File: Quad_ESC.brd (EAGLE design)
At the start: 96.5 x 39.9 mm, 28 parts, among them Y1 ECS-80-S-4X

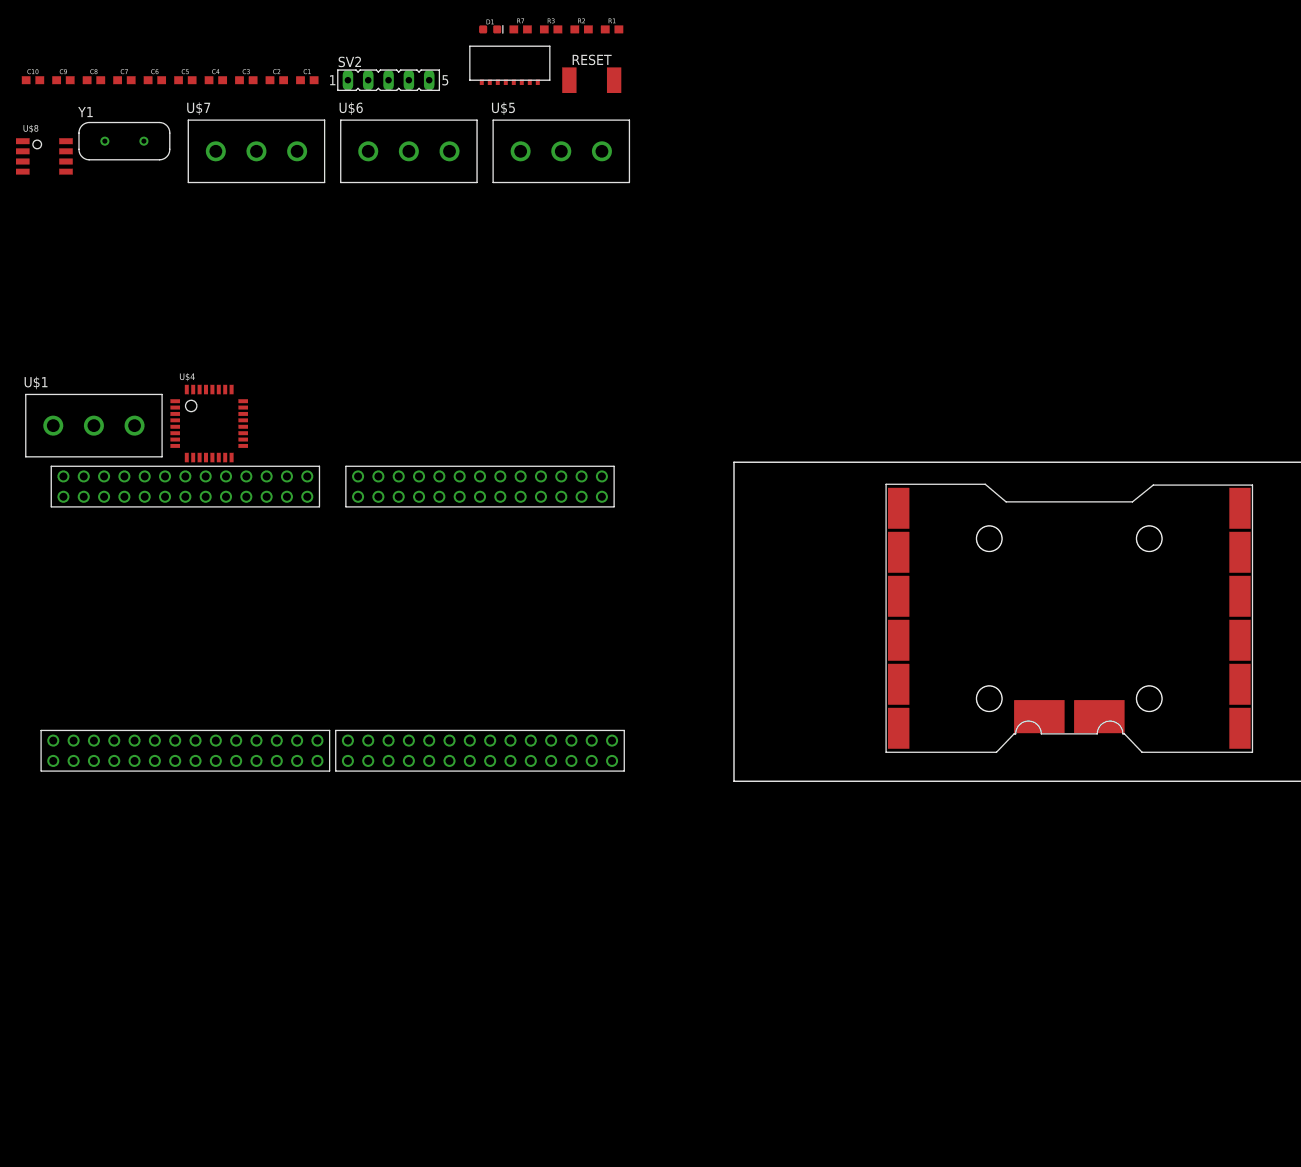
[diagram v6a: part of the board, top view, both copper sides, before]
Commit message: Schem/Lib Update
added new footprint to schematic and library, added ID resistor to chip, standardized symbols across schematic
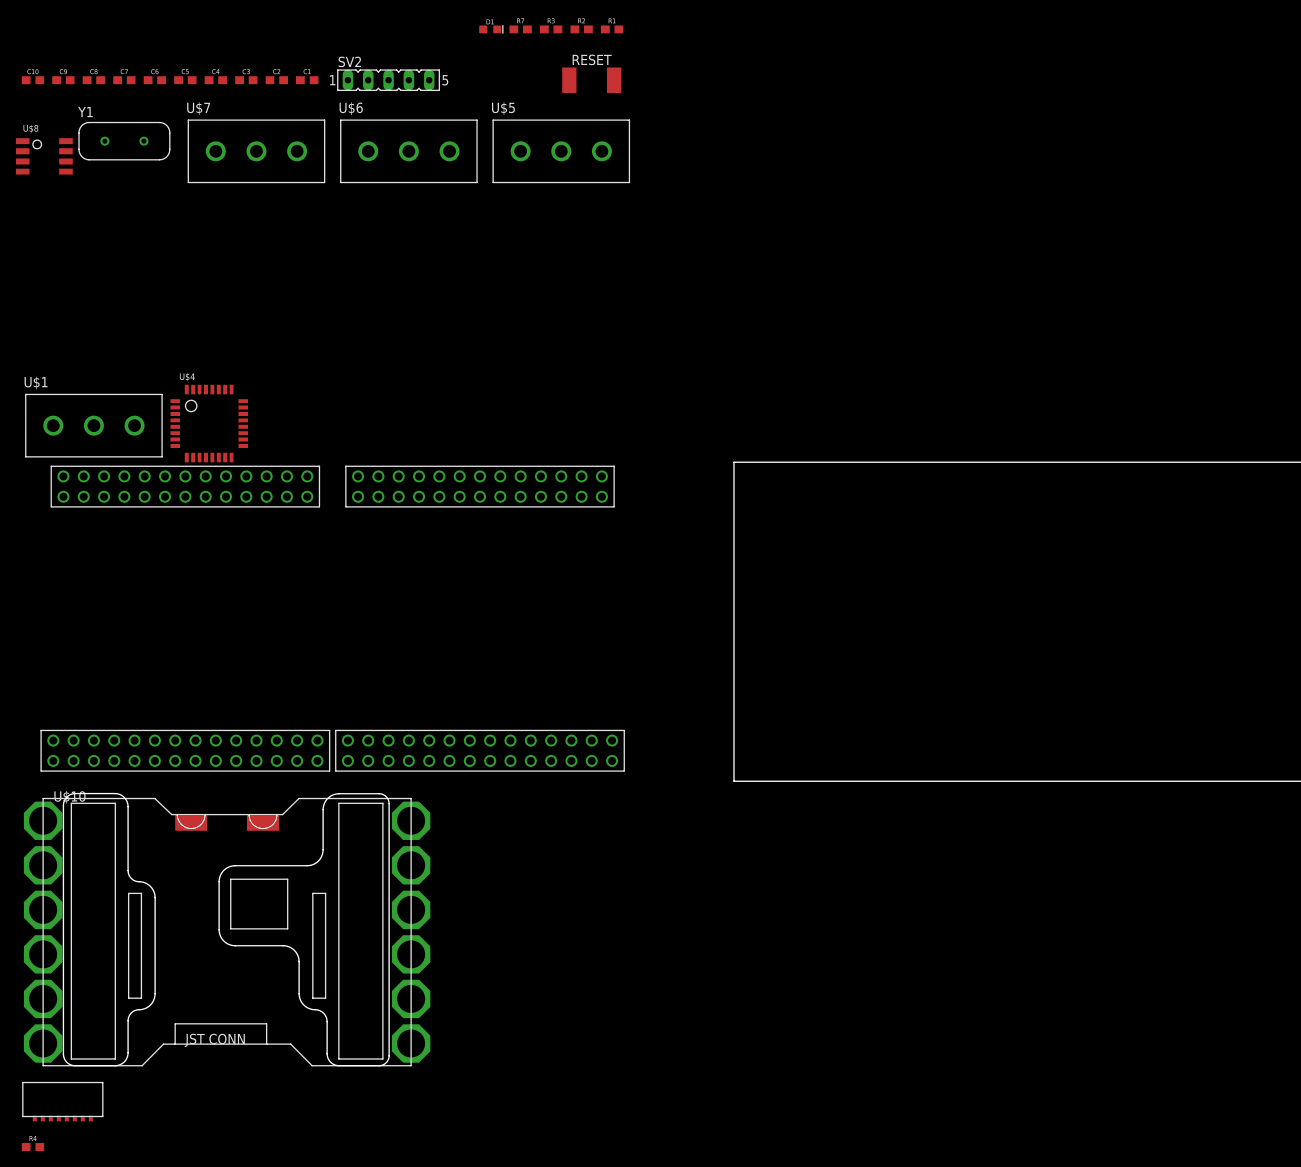
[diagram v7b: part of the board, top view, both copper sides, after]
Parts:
- added R4: 10k, SparkFun-Resistors:0603
- R7: value 470 -> (none)
- U$10: value BL_HELI45A -> LUMENIER_QUAD; device BLHeli_32 45A:BLHELI_20X20 -> BLHeli_32 45A:LUMENIER_QUAD
- moved U$9 141.1 mm to (-88.9, -41.9)
- moved U$10 139.9 mm to (-86.4, -35.6)
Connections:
- removed net OSC_IN1: U$4.PF0-OSC_IN
- removed net OSC_OUT1: U$4.PF1-OSC_OUT
- new net 3.3V: R4.1
- net +12V: now also U$10.VIN; no longer U$10.P$14
- net ESC1_B: now also U$10.1; no longer U$10.P$1
- net ESC1_R: now also U$10.3; no longer U$10.P$3
- net ESC1_Y: now also U$10.2; no longer U$10.P$2
- net ESC2_B: now also U$10.4; no longer U$10.P$4
- net ESC2_R: now also U$10.6; no longer U$10.P$6
- net ESC2_Y: now also U$10.5; no longer U$10.P$5
- net ESC3_B: now also U$10.12; no longer U$10.P$7
- net ESC3_R: now also U$10.10; no longer U$10.P$9
- net ESC3_Y: now also U$10.11; no longer U$10.P$8
- net ESC4_B: now also U$10.9; no longer U$10.P$10
- net ESC4_R: now also U$10.7; no longer U$10.P$12
- net ESC4_Y: now also U$10.8; no longer U$10.P$11
- net GND: now also R4.2, U$10.GND, U$4.PA3; no longer U$10.P$13
- net OSC_IN: now also U$4.PF0-OSC_IN
- net OSC_OUT: now also U$4.PF1-OSC_OUT

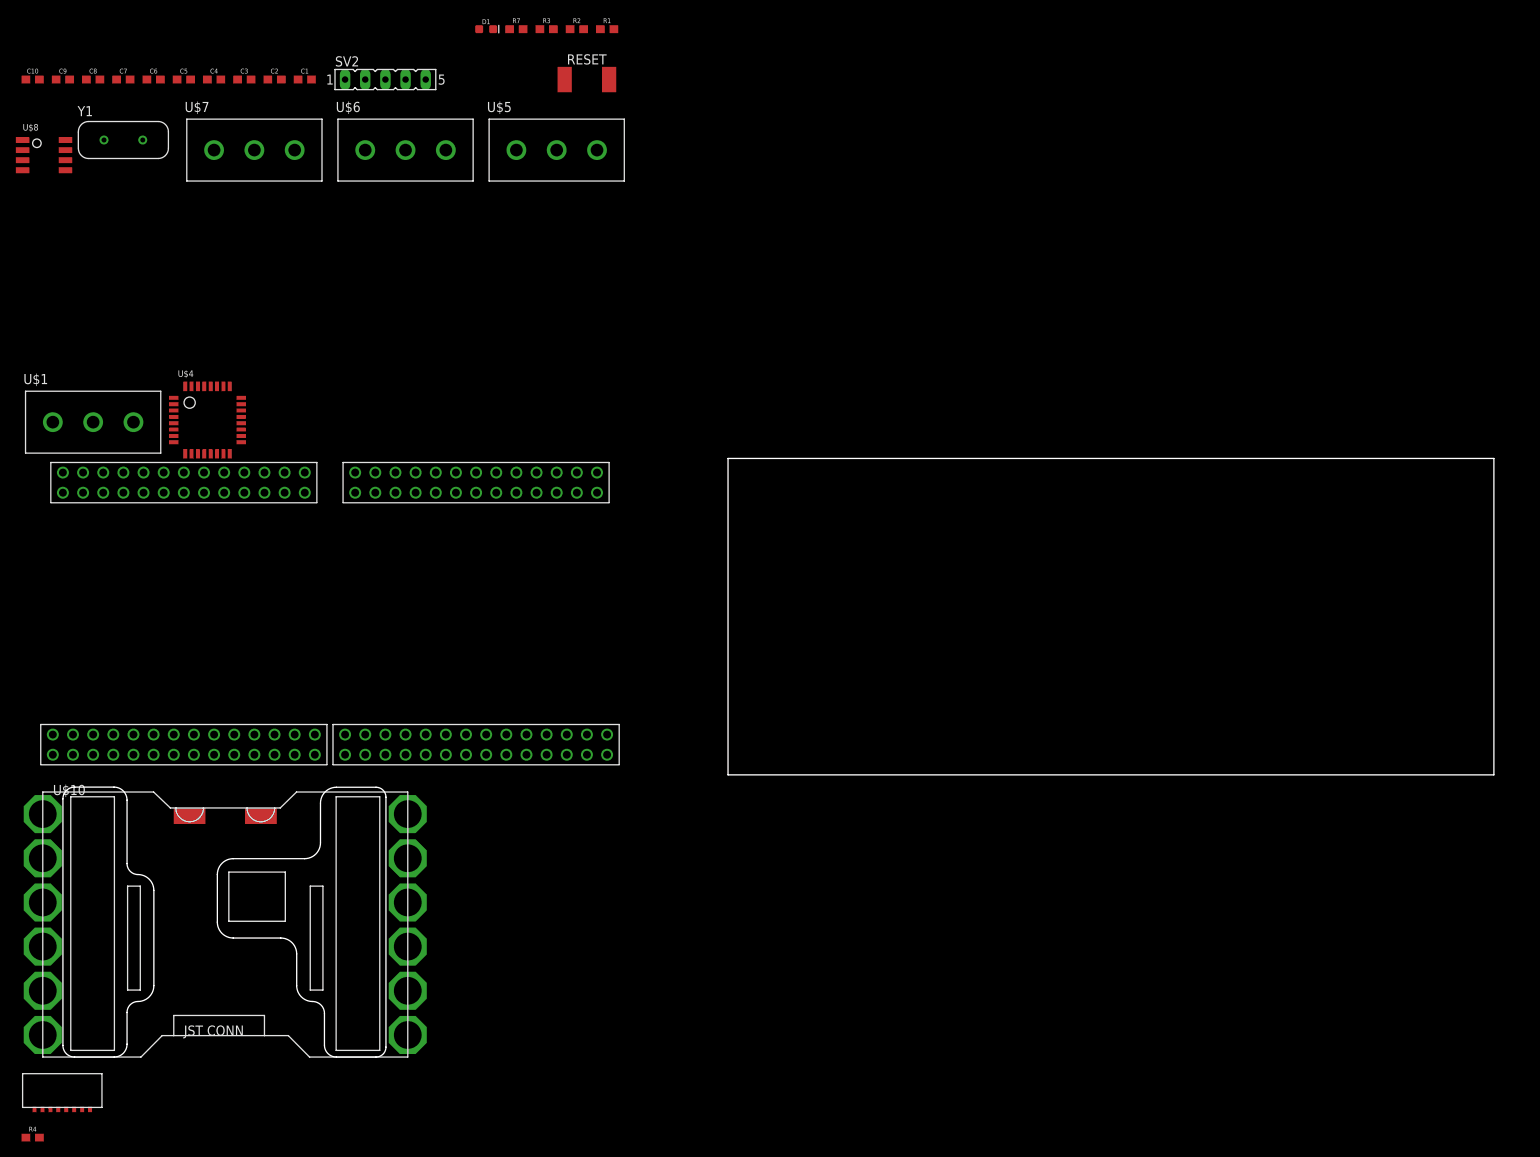
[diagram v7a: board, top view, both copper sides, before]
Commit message: Minor Sch Fixes/Board Placement
Fixed issues with schematic and doubling of backplane connectors, precursory board placements and connections
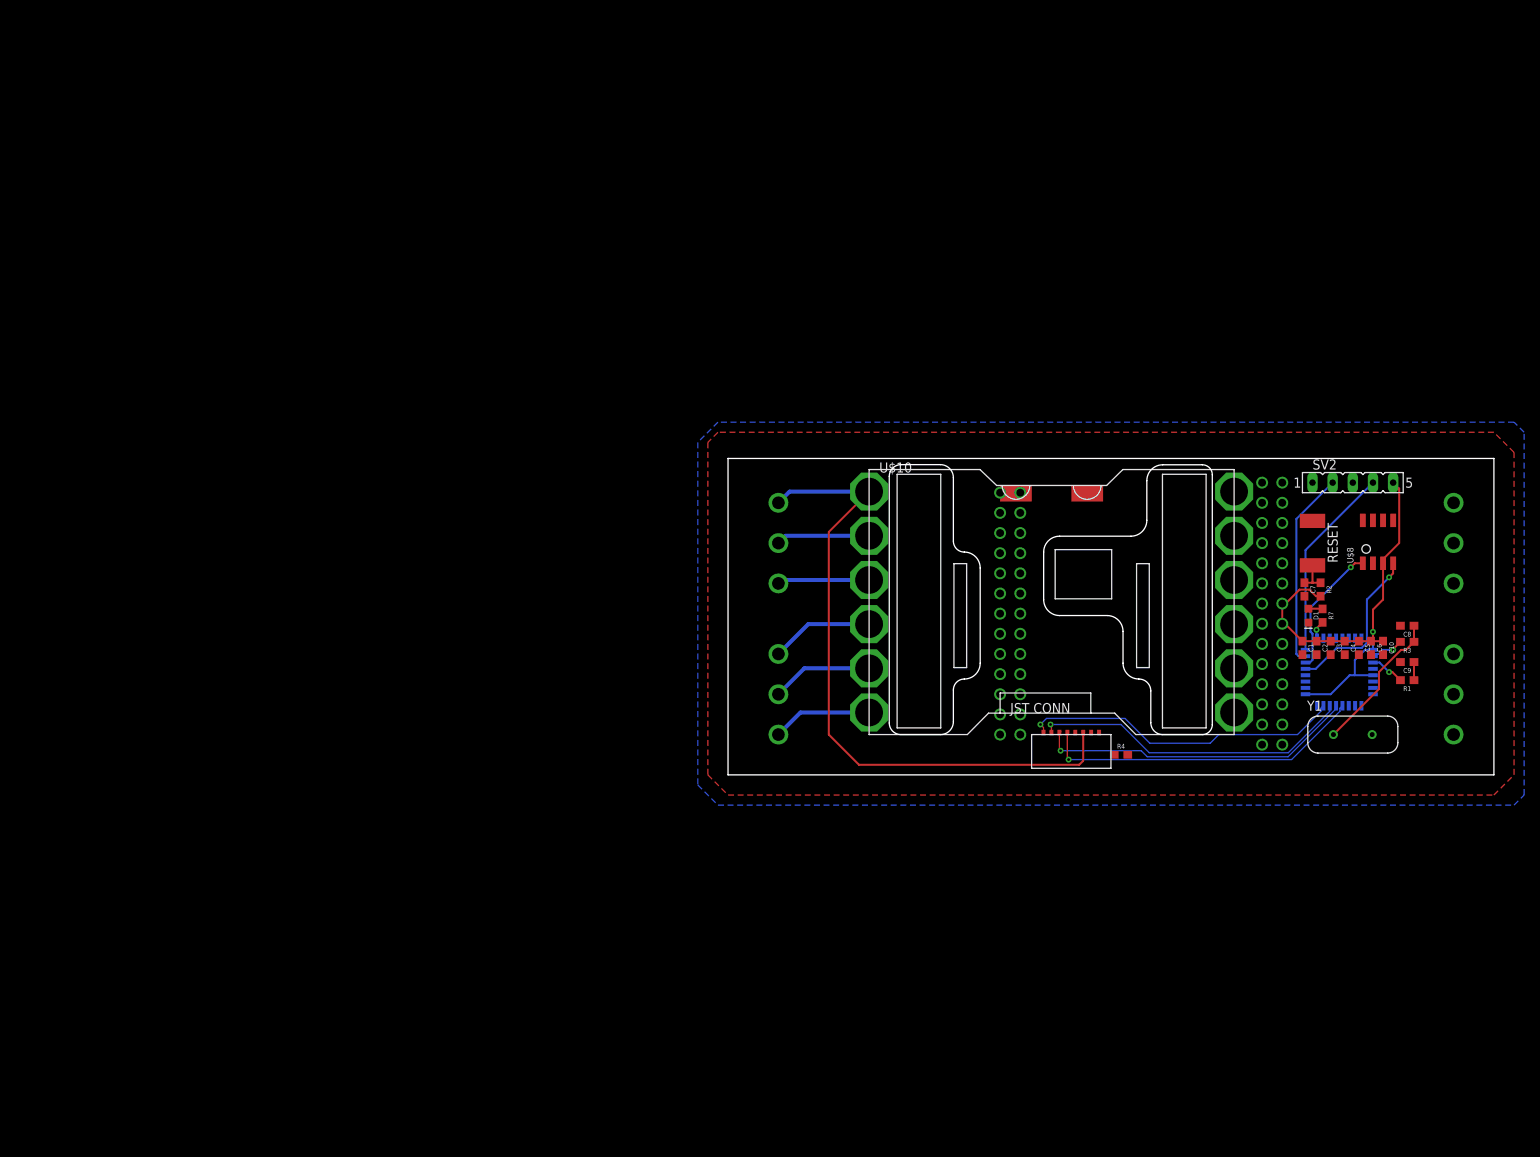
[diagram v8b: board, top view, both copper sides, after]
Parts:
- removed U$3: ESC2BACKPLANE, ESC_to_Backplane_Connectors:ESC2BACKPLANE_WHOLE
- moved C10 184.6 mm to (82.5, 16.0), turned to 270 degrees
- moved C9 184.6 mm to (85.6, 14.2), turned to 180 degrees
- moved U$8 179.7 mm to (83.8, 26.7), turned to 90 degrees
- moved C8 179.3 mm to (85.6, 18.8), turned to 180 degrees
- moved Y1 172.1 mm to (78.7, 5.08)
- moved C6 169.3 mm to (81.0, 16.0), turned to 270 degrees
- moved U$7 166.0 mm to (91.4, 10.2), flipped to the bottom, turned to 270 degrees
- moved C5 164.5 mm to (79.5, 16.0), turned to 270 degrees
- moved C7 162.1 mm to (72.6, 23.4), turned to 270 degrees
- moved C4 159.5 mm to (77.7, 16.0), turned to 270 degrees
- moved C3 154.5 mm to (75.9, 16.0), turned to 270 degrees
- moved U$4 154.4 mm to (81.3, 10.2), flipped to the bottom
- moved C2 149.6 mm to (74.2, 16.0), turned to 270 degrees
- moved R4 145.4 mm to (49.5, 2.54)
- moved U$9 145.0 mm to (48.3, 5.08), turned to 180 degrees
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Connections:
- new net N$10: U$2.P$7
- new net N$9: U$2.P$6
- net +12V: now also U$2.P$A, U$2.P$B, U$2.P$C, U$2.P$D, U$2.P$E, U$2.P$O, U$2.P$P, U$2.P$Q, U$2.P$R, U$2.P$S; no longer U$3.P$A, U$3.P$B, U$3.P$C, U$3.P$D, U$3.P$E, U$3.P$O, U$3.P$P, U$3.P$Q, U$3.P$R, U$3.P$S
- net +3V3: now also U$2.P$G, U$2.P$H, U$2.P$U, U$2.P$V; no longer U$3.P$G, U$3.P$H, U$3.P$U, U$3.P$V
- net CAN_H: no longer U$2.P$6
- net CAN_L: no longer U$2.P$7
- net GND: now also U$2.P$AA, U$2.P$BB, U$2.P$J, U$2.P$K, U$2.P$L, U$2.P$M, U$2.P$N, U$2.P$X, U$2.P$Y, U$2.P$Z; no longer U$3.P$AA, U$3.P$BB, U$3.P$J, U$3.P$K, U$3.P$L, U$3.P$M, U$3.P$N, U$3.P$X, U$3.P$Y, U$3.P$Z
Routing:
- net ESC1_B: track 0.00 -> 82.1 mm
- net +3V3: track 0.00 -> 60.3 mm, vias 0 -> 1
- net TIM3_CH1: track 0.00 -> 41.0 mm, vias 0 -> 1
- net TIM3_CH3: track 0.00 -> 40.8 mm, vias 0 -> 1
- net TIM3_CH4: track 0.00 -> 40.6 mm, vias 0 -> 1
- net TIM3_CH2: track 0.00 -> 40.5 mm, vias 0 -> 1
- net SWDIO: track 0.00 -> 24.8 mm
- net SWCLK: track 0.00 -> 24.6 mm
- net CAN_RX: track 0.00 -> 20.5 mm, vias 0 -> 1
- net N$2: track 0.00 -> 18.3 mm
- net CAN_TX: track 0.00 -> 16.6 mm, vias 0 -> 1
- net ESC2_B: track 0.00 -> 13.0 mm
- net ESC2_Y: track 0.00 -> 12.8 mm
- net ESC2_R: track 0.00 -> 12.6 mm
- net ESC1_Y: track 0.00 -> 11.8 mm
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- added copper zone on layer 1, net GND
- added copper zone on layer 16, net GND
